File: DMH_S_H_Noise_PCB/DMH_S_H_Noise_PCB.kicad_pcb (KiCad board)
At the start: 2 copper layers, 48 x 175 mm, 0 parts

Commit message: Component placement ongoing
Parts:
- added C1: 47uF, Capacitor_THT:CP_Radial_D5.0mm_P2.00mm, B.Cu at (80.0, 52.0)
- added C10: 1nF, Capacitor_THT:C_Disc_D4.3mm_W1.9mm_P5.00mm, B.Cu at (132.5, 59.2)
- added C11: 100nF, Capacitor_THT:C_Disc_D4.3mm_W1.9mm_P5.00mm, B.Cu at (141.8, 62.5)
- added C12: 1uF, Capacitor_THT:C_Disc_D4.3mm_W1.9mm_P5.00mm, B.Cu at (132.5, 66.2)
- added C13: 1uF, Capacitor_THT:C_Disc_D4.3mm_W1.9mm_P5.00mm, B.Cu at (132.5, 69.6)
- added C14: 680pF, Capacitor_THT:C_Disc_D4.3mm_W1.9mm_P5.00mm, B.Cu at (132.5, 73.0)
- added C15: 2.2nF, Capacitor_THT:C_Disc_D4.3mm_W1.9mm_P5.00mm, B.Cu at (132.5, 76.5)
- added C16: 5.6nF, Capacitor_THT:C_Disc_D4.3mm_W1.9mm_P5.00mm, B.Cu at (132.5, 80.0)
- added C17: 680pF, Capacitor_THT:C_Disc_D4.3mm_W1.9mm_P5.00mm, B.Cu at (132.5, 83.4)
- added C18: 2.2nF, Capacitor_THT:C_Disc_D4.3mm_W1.9mm_P5.00mm, B.Cu at (132.5, 86.8)
- added C19: 5.6nF, Capacitor_THT:C_Disc_D4.3mm_W1.9mm_P5.00mm, B.Cu at (132.5, 90.3)
- added C2: 47uF, Capacitor_THT:CP_Radial_D5.0mm_P2.00mm, B.Cu at (86.5, 52.0)
- added C20: 100nF, Capacitor_THT:C_Disc_D4.3mm_W1.9mm_P5.00mm, B.Cu at (65.2, 101.8)
- added C21: 100nF, Capacitor_THT:C_Disc_D4.3mm_W1.9mm_P5.00mm, B.Cu at (65.2, 80.8)
- added C3: 100nF, Capacitor_THT:C_Disc_D4.3mm_W1.9mm_P5.00mm, B.Cu at (79.8, 58.0)
- added C4: 100nF, Capacitor_THT:C_Disc_D4.3mm_W1.9mm_P5.00mm, B.Cu at (87.0, 58.0)
- added C5: 100nF, Capacitor_THT:C_Disc_D4.3mm_W1.9mm_P5.00mm, B.Cu at (90.2, 80.8)
- added C6: 100nF, Capacitor_THT:C_Disc_D4.3mm_W1.9mm_P5.00mm, B.Cu at (90.2, 101.8)
- added C7: 100nF, Capacitor_THT:C_Disc_D4.3mm_W1.9mm_P5.00mm, B.Cu at (64.5, 122.8)
- added C8: 100nF, Capacitor_THT:C_Disc_D4.3mm_W1.9mm_P5.00mm, B.Cu at (85.5, 122.8)
- added C9: 1uF, Capacitor_THT:C_Disc_D4.3mm_W1.9mm_P5.00mm, B.Cu at (41.5, 51.5)
- added D1: LED, LED_THT:LED_D3.0mm, F.Cu at (73.7, 47.5)
- added D2: 1N4148, Diode_THT:D_DO-35_SOD27_P7.62mm_Horizontal, B.Cu at (38.6, 119.2)
- added D3: 1N4148, Diode_THT:D_DO-35_SOD27_P7.62mm_Horizontal, B.Cu at (38.6, 122.7)
- added D4: SB140-, Diode_THT:D_DO-41_SOD81_P10.16mm_Horizontal, B.Cu at (97.6, 65.8)
- added D5: SB140+, Diode_THT:D_DO-41_SOD81_P10.16mm_Horizontal, B.Cu at (77.3, 44.2)
- added D6: 1N4148, Diode_THT:D_DO-35_SOD27_P7.62mm_Horizontal, B.Cu at (38.6, 126.2)
- added J0: Conn_01x01, Connector_PinHeader_2.54mm:PinHeader_1x01_P2.54mm_Vertical, F.Cu at (55.0, 72.5)
- added J1: TS_Jack_6.35mm_Sw, SynthStuff:CUI_MJ-63052A, F.Cu at (58.5, 171.8)
- added J100: IDC_02x05, SynthStuff:IDC-Header_2x05_P2.54mm_Vertical_Eurorack, B.Cu at (92.7, 58.3)
- added J2: TS_Jack_6.35mm_Sw, SynthStuff:CUI_MJ-63052A, F.Cu at (58.5, 190.2)
- added J200: IDC_02x05, SynthStuff:IDC-Header_2x05_P2.54mm_Vertical_BackBone, B.Cu at (93.3, 155.3)
- added J3: TS_Jack_6.35mm_Sw, SynthStuff:CUI_MJ-63052A, F.Cu at (75.0, 171.8)
- added J4: TS_Jack_6.35mm_Sw, SynthStuff:CUI_MJ-63052A, F.Cu at (75.0, 190.2)
- added J5: TS_Jack_6.35mm_Sw, SynthStuff:CUI_MJ-63052A, F.Cu at (91.5, 171.8)
- added J50: Conn_01x06, Connector_PinHeader_2.54mm:PinHeader_1x06_P2.54mm_Vertical, F.Cu at (64.8, 161.5)
- added J6: TS_Jack_6.35mm_Sw, SynthStuff:CUI_MJ-63052A, F.Cu at (91.5, 190.2)
- added J60: Conn_01x06, Connector_PinHeader_2.54mm:PinHeader_1x06_P2.54mm_Vertical, F.Cu at (81.3, 161.5)
- added J7: TS_Jack_6.35mm_Sw, SynthStuff:CUI_MJ-63052A, F.Cu at (58.5, 208.8)
- added J70: Conn_01x06, Connector_PinHeader_2.54mm:PinHeader_1x06_P2.54mm_Vertical, F.Cu at (97.9, 161.5)
- added J8: TS_Jack_6.35mm_Sw, SynthStuff:CUI_MJ-63052A, F.Cu at (75.0, 208.8)
- added J9: TS_Jack_6.35mm_Sw, SynthStuff:CUI_MJ-63052A, F.Cu at (91.5, 208.8)
- added Q1: BC548, Package_TO_SOT_THT:TO-92_Inline_Wide, B.Cu at (111.2, 125.5)
- added Q2: J113, Package_TO_SOT_THT:TO-92L_Inline, B.Cu at (110.0, 116.7)
- added Q3: BC548, Package_TO_SOT_THT:TO-92_Inline_Wide, B.Cu at (110.8, 133.2)
- added R1: 100k, Resistor_THT:R_Axial_DIN0207_L6.3mm_D2.5mm_P7.62mm_Horizontal, B.Cu at (44.1, 60.7)
- added R10: 100k, Resistor_THT:R_Axial_DIN0207_L6.3mm_D2.5mm_P7.62mm_Horizontal, B.Cu at (151.1, 175.2)
- added R11: 1M, Resistor_THT:R_Axial_DIN0207_L6.3mm_D2.5mm_P7.62mm_Horizontal, B.Cu at (140.3, 138.8)
- added R12: 1k, Resistor_THT:R_Axial_DIN0207_L6.3mm_D2.5mm_P7.62mm_Horizontal, B.Cu at (140.3, 142.8)
- added R13: 1k, Resistor_THT:R_Axial_DIN0207_L6.3mm_D2.5mm_P7.62mm_Horizontal, B.Cu at (140.3, 146.9)
- added R14: 100k, Resistor_THT:R_Axial_DIN0207_L6.3mm_D2.5mm_P7.62mm_Horizontal, B.Cu at (140.3, 150.9)
- added R15: 100k, Resistor_THT:R_Axial_DIN0207_L6.3mm_D2.5mm_P7.62mm_Horizontal, B.Cu at (140.3, 155.0)
- added R16: 270R, Resistor_THT:R_Axial_DIN0207_L6.3mm_D2.5mm_P7.62mm_Horizontal, B.Cu at (140.3, 159.1)
- added R17: 100k, Resistor_THT:R_Axial_DIN0207_L6.3mm_D2.5mm_P7.62mm_Horizontal, B.Cu at (140.3, 163.1)
- added R18: 1k, Resistor_THT:R_Axial_DIN0207_L6.3mm_D2.5mm_P7.62mm_Horizontal, B.Cu at (140.3, 167.2)
- added R19: 100k, Resistor_THT:R_Axial_DIN0207_L6.3mm_D2.5mm_P7.62mm_Horizontal, B.Cu at (140.3, 171.2)
- added R2: 2k, Resistor_THT:R_Axial_DIN0207_L6.3mm_D2.5mm_P7.62mm_Horizontal, B.Cu at (44.1, 64.8)
- added R20: 4k7, Resistor_THT:R_Axial_DIN0207_L6.3mm_D2.5mm_P7.62mm_Horizontal, B.Cu at (140.3, 175.2)
- added R21: 47k, Resistor_THT:R_Axial_DIN0207_L6.3mm_D2.5mm_P7.62mm_Horizontal, B.Cu at (129.5, 138.8)
- added R22: 470k, Resistor_THT:R_Axial_DIN0207_L6.3mm_D2.5mm_P7.62mm_Horizontal, B.Cu at (129.5, 142.8)
- added R23: 22k, Resistor_THT:R_Axial_DIN0207_L6.3mm_D2.5mm_P7.62mm_Horizontal, B.Cu at (129.5, 146.9)
- added R24: 100k, Resistor_THT:R_Axial_DIN0207_L6.3mm_D2.5mm_P7.62mm_Horizontal, B.Cu at (129.5, 150.9)
- added R25: 1k, Resistor_THT:R_Axial_DIN0207_L6.3mm_D2.5mm_P7.62mm_Horizontal, B.Cu at (129.5, 155.0)
- added R26: 1M, Resistor_THT:R_Axial_DIN0207_L6.3mm_D2.5mm_P7.62mm_Horizontal, B.Cu at (129.5, 159.1)
- added R27: 470k, Resistor_THT:R_Axial_DIN0207_L6.3mm_D2.5mm_P7.62mm_Horizontal, B.Cu at (129.5, 163.1)
- added R28: 10k, Resistor_THT:R_Axial_DIN0207_L6.3mm_D2.5mm_P7.62mm_Horizontal, B.Cu at (129.5, 167.2)
- added R29: 20k, Resistor_THT:R_Axial_DIN0207_L6.3mm_D2.5mm_P7.62mm_Horizontal, B.Cu at (129.5, 171.2)
- added R3: 100k, Resistor_THT:R_Axial_DIN0207_L6.3mm_D2.5mm_P7.62mm_Horizontal, B.Cu at (44.1, 68.8)
- added R30: 10k, Resistor_THT:R_Axial_DIN0207_L6.3mm_D2.5mm_P7.62mm_Horizontal, B.Cu at (129.5, 175.2)
- added R31: 100K, Resistor_THT:R_Axial_DIN0207_L6.3mm_D2.5mm_P7.62mm_Horizontal, B.Cu at (118.8, 138.8)
- added R32: 1k, Resistor_THT:R_Axial_DIN0207_L6.3mm_D2.5mm_P7.62mm_Horizontal, B.Cu at (118.8, 142.8)
- added R33: 1k, Resistor_THT:R_Axial_DIN0207_L6.3mm_D2.5mm_P7.62mm_Horizontal, B.Cu at (118.8, 146.9)
- added R34: 100k, Resistor_THT:R_Axial_DIN0207_L6.3mm_D2.5mm_P7.62mm_Horizontal, B.Cu at (118.8, 150.9)
- added R35: 10k, Resistor_THT:R_Axial_DIN0207_L6.3mm_D2.5mm_P7.62mm_Horizontal, B.Cu at (118.8, 155.0)
- added R36: 100k, Resistor_THT:R_Axial_DIN0207_L6.3mm_D2.5mm_P7.62mm_Horizontal, B.Cu at (118.8, 159.1)
- added R37: 100k, Resistor_THT:R_Axial_DIN0207_L6.3mm_D2.5mm_P7.62mm_Horizontal, B.Cu at (118.8, 163.1)
- added R38: 100k, Resistor_THT:R_Axial_DIN0207_L6.3mm_D2.5mm_P7.62mm_Horizontal, B.Cu at (118.8, 167.2)
- added R4: 100k, Resistor_THT:R_Axial_DIN0207_L6.3mm_D2.5mm_P7.62mm_Horizontal, B.Cu at (151.1, 150.9)
- added R5: 51k, Resistor_THT:R_Axial_DIN0207_L6.3mm_D2.5mm_P7.62mm_Horizontal, B.Cu at (151.1, 155.0)
- added R6: 2k, Resistor_THT:R_Axial_DIN0207_L6.3mm_D2.5mm_P7.62mm_Horizontal, B.Cu at (151.1, 159.1)
- added R7: 100k, Resistor_THT:R_Axial_DIN0207_L6.3mm_D2.5mm_P7.62mm_Horizontal, B.Cu at (151.1, 163.1)
- added R8: 100k, Resistor_THT:R_Axial_DIN0207_L6.3mm_D2.5mm_P7.62mm_Horizontal, B.Cu at (151.1, 167.2)
- added R9: 33k, Resistor_THT:R_Axial_DIN0207_L6.3mm_D2.5mm_P7.62mm_Horizontal, B.Cu at (151.1, 171.2)
- added RV1: 250k, Potentiometer_THT:Potentiometer_Alpha_RD901F-40-00D_Single_Vertical, F.Cu at (72.5, 78.5)
- added RV2: 100k, Potentiometer_THT:Potentiometer_Alpha_RD901F-40-00D_Single_Vertical, F.Cu at (60.0, 115.7)
- added RV3: 100k, Potentiometer_THT:Potentiometer_Alpha_RD901F-40-00D_Single_Vertical, F.Cu at (85.0, 115.7)
- added SW1: SW_Push, Button_Switch_Keyboard:SW_Cherry_MX_1.00u_PCB, F.Cu at (90.0, 137.4)
- added SW2: SW_SPDT_321, SynthStuff:Toggle_Switch_THT, F.Cu at (62.5, 142.5)
- added U1: TL074, Package_DIP:DIP-14_W7.62mm_Socket, B.Cu at (91.5, 83.6)
- added U2: TL074, Package_DIP:DIP-14_W7.62mm_Socket, B.Cu at (67.4, 121.5)
- added U3: TL074, Package_DIP:DIP-14_W7.62mm_Socket, B.Cu at (66.5, 83.6)

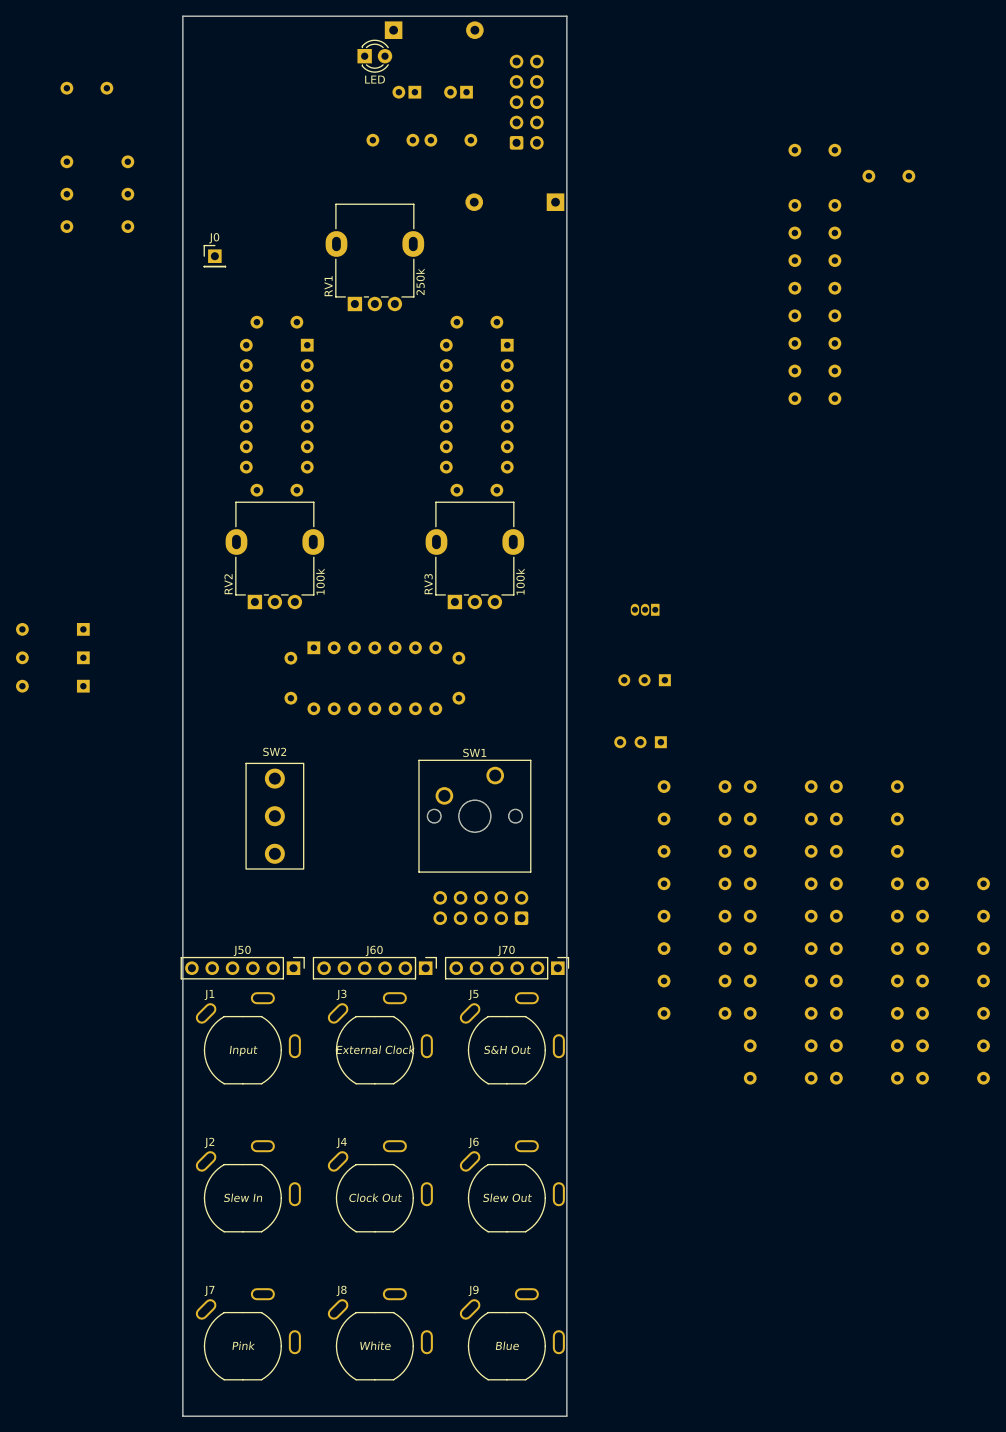
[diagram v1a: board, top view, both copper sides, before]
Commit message: Finished placement and initial routing
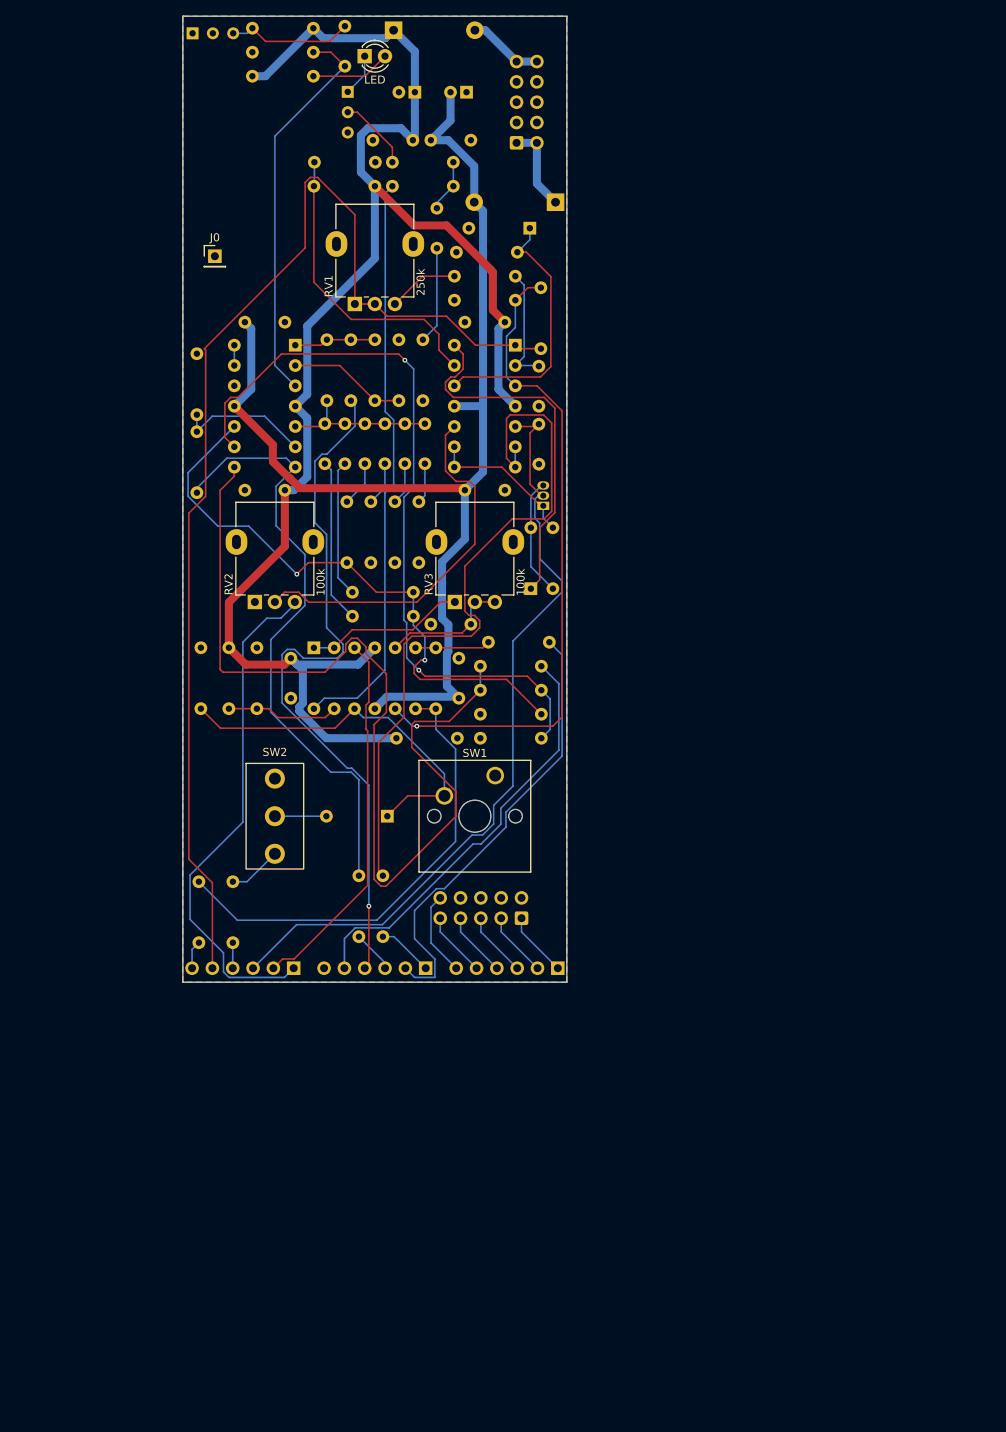
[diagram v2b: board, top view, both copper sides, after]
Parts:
- removed J1, J2, J3, J4, J5, J6, J7, J8, J9: TS_Jack_6.35mm_Sw, SynthStuff:CUI_MJ-63052A
- J50, J60, J70: moved to B.Cu
- moved R6 142.3 mm to (59.7, 50.0), turned to 0 degrees
- moved R9 138.5 mm to (67.4, 60.8), turned to 0 degrees
- moved R10 135.0 mm to (75.0, 63.8)
- moved R15 130.4 mm to (67.3, 47.0)
- moved R14 129.5 mm to (67.3, 44.0)
- moved R5 119.8 mm to (77.2, 60.8), turned to 0 degrees
- moved R8 111.6 mm to (92.8, 72.0)
- moved R19 107.6 mm to (69.0, 90.6), turned to 90 degrees
- moved R7 106.5 mm to (81.0, 82.9), turned to -90 degrees
- moved Q3 106.2 mm to (52.2, 44.6), turned to 0 degrees
- moved R36 104.0 mm to (77.2, 63.8), turned to 0 degrees
- moved R17 103.4 mm to (75.0, 82.9), turned to -90 degrees
- moved R18 102.6 mm to (72.0, 90.6), turned to 90 degrees
- moved R24 95.3 mm to (52.8, 94.4), turned to -90 degrees
- moved R23 94.2 mm to (52.8, 92.3), turned to 90 degrees
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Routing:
- net +12V: track 0.00 -> 197.2 mm
- net /Core Circuit/Internal Clock: track 0.00 -> 150.7 mm
- net -12V: track 0.00 -> 144.9 mm
- net Net-(R31-Pad2): track 0.00 -> 119.2 mm
- net /Core Circuit/S&H: track 0.00 -> 97.6 mm
- net Net-(U3C--): track 0.00 -> 95.1 mm, vias 0 -> 2
- net Net-(U1B--): track 0.00 -> 89.7 mm
- net /Core Circuit/White: track 0.00 -> 88.4 mm, vias 0 -> 1
- net Net-(U1A-+): track 0.00 -> 83.1 mm, vias 0 -> 1
- net Net-(R24-Pad2): track 0.00 -> 76.2 mm
- net Net-(U3C-+): track 0.00 -> 75.1 mm, vias 0 -> 2
- net Net-(R36-Pad1): track 0.00 -> 72.7 mm
- net /Core Circuit/Input: track 0.00 -> 64.0 mm
- net Net-(U2C--): track 0.00 -> 58.7 mm
- net /Core Circuit/Slew Output: track 0.00 -> 56.0 mm
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- added copper zone on B.Cu, net GND
- added copper zone on F.Cu, net GND
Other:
- board size 48 x 175 mm -> 48 x 120.8 mm
